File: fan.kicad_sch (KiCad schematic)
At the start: 18 parts, among them J5 Conn_01x04, J6 Conn_01x04, U16 TMP1075, U17 TMP1075, U18 EMC2302

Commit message: Resolved all unconnected pins, re-annotated, reviewed for layout
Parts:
- renumbered C62 to C31, C63 to C32, C64 to C33, C65 to C34, C66 to C35, C67 to C36, C68 to C37, R40 to R20, R41 to R21, TP9 to TP17, TP10 to TP18, TP11 to TP19, TP12 to TP20, U16 to U10, U17 to U11, U18 to U12

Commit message: Rough parts placement
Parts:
- TP17, TP18, TP19, TP20: footprint TestPoint:TestPoint_Pad_D1.5mm -> TestPoint:TestPoint_Pad_D1.0mm
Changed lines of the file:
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@@
       (effects (font (size 1.27 1.27)) (justify left) hide)
     )
-    (property "Footprint" "TestPoint:TestPoint_Pad_D1.5mm" (at 229.235 53.34 0)
+    (property "Footprint" "TestPoint:TestPoint_Pad_D1.0mm" (at 229.235 53.34 0)
       (effects (font (size 1.27 1.27)) hide)
     )
@@
       (effects (font (size 1.27 1.27)) (justify left) hide)
     )
-    (property "Footprint" "TestPoint:TestPoint_Pad_D1.5mm" (at 229.235 86.36 0)
+    (property "Footprint" "TestPoint:TestPoint_Pad_D1.0mm" (at 229.235 86.36 0)
       (effects (font (size 1.27 1.27)) hide)
     )
@@
       (effects (font (size 1.27 1.27)) (justify left) hide)
     )
-    (property "Footprint" "TestPoint:TestPoint_Pad_D1.5mm" (at 195.58 55.88 0)
+    (property "Footprint" "TestPoint:TestPoint_Pad_D1.0mm" (at 195.58 55.88 0)
       (effects (font (size 1.27 1.27)) hide)
     )
@@
       (effects (font (size 1.27 1.27)) (justify left) hide)
     )
-    (property "Footprint" "TestPoint:TestPoint_Pad_D1.5mm" (at 195.58 88.9 0)
-      (effects (font (size 1.27 1.27)) hide)
-    )
+    (property "Footprint" "TestPoint:TestPoint_Pad_D1.0mm" (at 195.58 88.9 0)
+      (effects (font (size 1.27 1.27)) hide)
+    )

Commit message: added some DK part numbers
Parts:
- U12: DK (none) -> EMC2302-2-AIZL-CT-ND; PARTNO (none) -> EMC2302-2-AIZL-TR
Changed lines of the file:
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@@
       (effects (font (size 1.27 1.27) italic) hide)
+    )
+    (property "DK" "EMC2302-2-AIZL-CT-ND" (at 89.535 52.07 0)
+      (effects (font (size 1.27 1.27)) hide)
+    )
+    (property "PARTNO" "EMC2302-2-AIZL-TR" (at 89.535 52.07 0)
+      (effects (font (size 1.27 1.27)) hide)
     )
     (pin "1")

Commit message: BOM mostly completed
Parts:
- R20, R21: DK (none) -> 13-RC0402FR-135K6LCT-ND; PARTNO (none) -> RC0402FR-135K6L
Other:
- title: bitaxeUltraHex -> bitaxeHex
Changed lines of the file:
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@@
   (paper "A")
   (title_block
-    (title "bitaxeUltraHex")
+    (title "bitaxeHex")
     (date "2023-06-11")
-    (rev "1")
+    (rev "300")
   )
   (junction (at 205.105 99.695) (diameter 0) (color 0 0 0 0)
@@
       (effects (font (size 1.27 1.27)) hide)
     )
-    (property "DK" "" (at 207.645 45.72 0)
-      (effects (font (size 1.27 1.27)) hide)
-    )
-    (property "PARTNO" "" (at 207.645 45.72 0)
+    (property "DK" "13-RC0402FR-135K6LCT-ND" (at 207.645 45.72 0)
+      (effects (font (size 1.27 1.27)) hide)
+    )
+    (property "PARTNO" "RC0402FR-135K6L" (at 207.645 45.72 0)
       (effects (font (size 1.27 1.27)) hide)
     )
@@
       (effects (font (size 1.27 1.27)) hide)
     )
-    (property "DK" "" (at 207.645 78.74 0)
-      (effects (font (size 1.27 1.27)) hide)
-    )
-    (property "PARTNO" "" (at 207.645 78.74 0)
-      (effects (font (size 1.27 1.27)) hide)
-    )
+    (property "DK" "13-RC0402FR-135K6LCT-ND" (at 207.645 78.74 0)
+      (effects (font (size 1.27 1.27)) hide)
+    )
+    (property "PARTNO" "RC0402FR-135K6L" (at 207.645 78.74 0)
+      (effects (font (size 1.27 1.27)) hide)
+    )

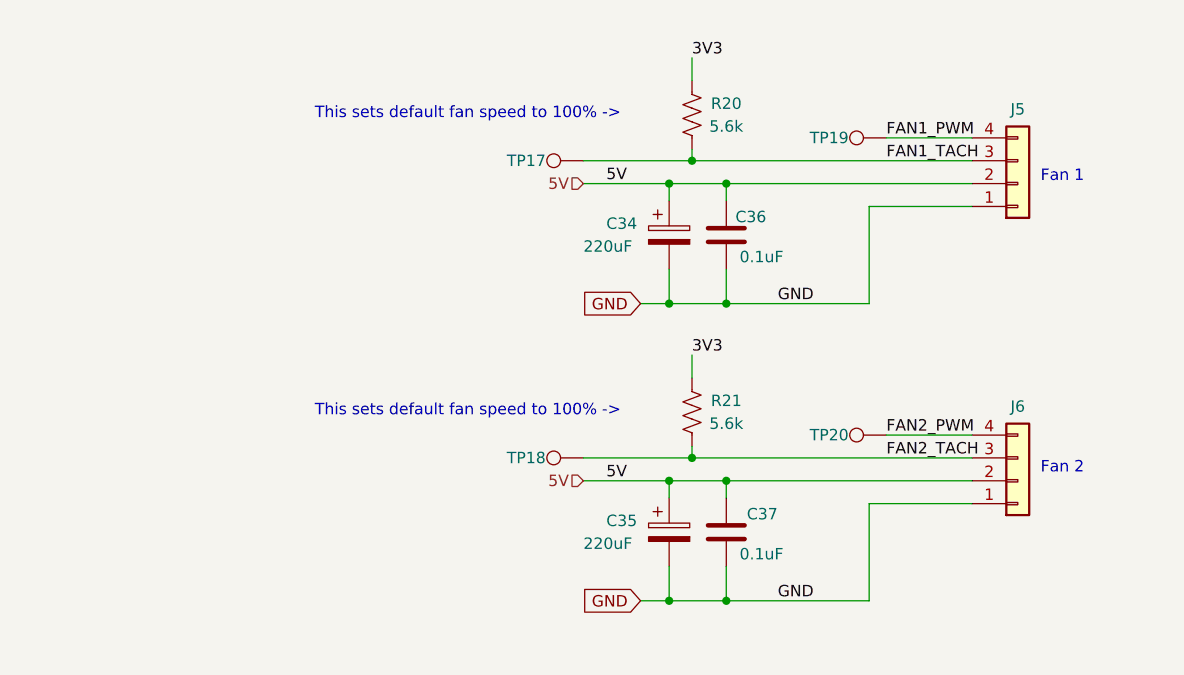
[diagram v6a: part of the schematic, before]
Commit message: remove old 5V power supply, prepare footprints for new 5V buck supply, switch fans to 12V
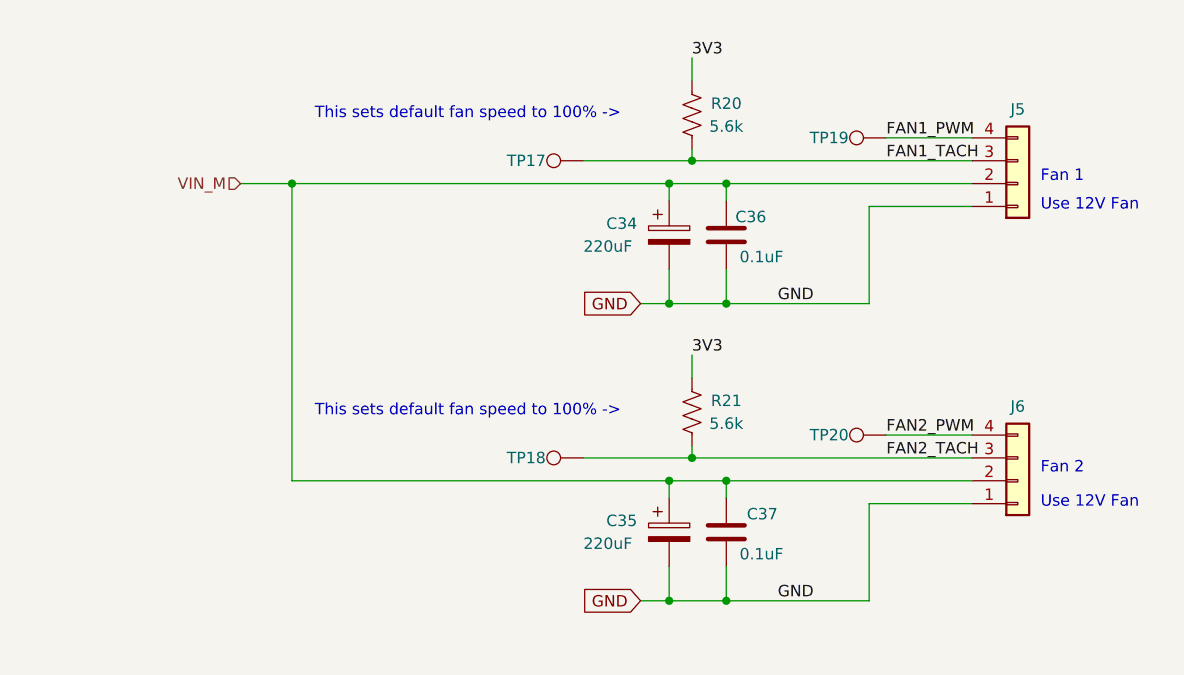
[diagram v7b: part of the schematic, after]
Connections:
- net 5V renamed VIN_M
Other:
- note added: "Use 12V Fan"
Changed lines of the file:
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@@
   (junction (at 105.41 120.65) (diameter 0) (color 0 0 0 0)
   )
+  (junction (at 163.195 53.34) (diameter 0) (color 0 0 0 0)
+  )
   (junction (at 105.41 137.795) (diameter 0) (color 0 0 0 0)
   )
@@
     (stroke (width 0) (type default))
   )
+  (wire (pts (xy 163.195 53.34) (xy 205.105 53.34))
+    (stroke (width 0) (type default))
+  )
   (wire (pts (xy 211.455 86.36) (xy 211.455 88.265))
     (stroke (width 0) (type default))
@@
     (stroke (width 0) (type default))
   )
+  (wire (pts (xy 163.195 86.36) (xy 163.195 53.34))
+    (stroke (width 0) (type default))
+  )
   (wire (pts (xy 211.455 99.695) (xy 227.33 99.695))
     (stroke (width 0) (type default))
@@
     (stroke (width 0) (type default))
   )
-  (wire (pts (xy 195.58 53.34) (xy 205.105 53.34))
+  (wire (pts (xy 157.48 53.34) (xy 163.195 53.34))
     (stroke (width 0) (type default))
   )
@@
     (stroke (width 0) (type default))
   )
-  (wire (pts (xy 195.58 86.36) (xy 205.105 86.36))
+  (wire (pts (xy 163.195 86.36) (xy 205.105 86.36))
     (stroke (width 0) (type default))
   )
@@
     (effects (font (size 1.27 1.27)) (justify left bottom))
   )
+  (text "Use 12V Fan" (at 246.38 56.515 0)
+    (effects (font (size 1.27 1.27)) (justify left bottom))
+  )
+  (text "Use 12V Fan" (at 246.38 89.535 0)
+    (effects (font (size 1.27 1.27)) (justify left bottom))
+  )
   (text "This sets default fan speed to 100% ->" (at 165.735 46.355 0)
     (effects (font (size 1.27 1.27)) (justify left bottom))
@@
     (effects (font (size 1.27 1.27)) (justify right bottom))
   )
-  (label "5V" (at 198.12 53.34 0) (fields_autoplaced)
-    (effects (font (size 1.27 1.27)) (justify left bottom))
-  )
   (label "3V3" (at 109.855 120.65 180) (fields_autoplaced)
     (effects (font (size 1.27 1.27)) (justify right bottom))
@@
   )
   (label "FAN2_PWM" (at 229.235 81.28 0) (fields_autoplaced)
-    (effects (font (size 1.27 1.27)) (justify left bottom))
-  )
-  (label "5V" (at 198.12 86.36 0) (fields_autoplaced)
     (effects (font (size 1.27 1.27)) (justify left bottom))
   )
@@
     )
   )
-  (hierarchical_label "5V" (shape input) (at 195.58 53.34 180) (fields_autoplaced)
+  (hierarchical_label "VIN_M" (shape input) (at 157.48 53.34 180) (fields_autoplaced)
     (effects (font (size 1.27 1.27)) (justify right))
   )
-  (hierarchical_label "5V" (shape input) (at 195.58 86.36 180) (fields_autoplaced)
-    (effects (font (size 1.27 1.27)) (justify right))
-  )

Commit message: BOM cleanup
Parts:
- C31, C32, C33, C36, C37: DK 1292-1639-1-ND -> 478-KGM05AR71C104KHCT-ND; PARTNO 0402X104K100CT -> KGM05AR71C104KH
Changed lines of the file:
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@@
       (effects (font (size 1.778 1.5113)) (justify left bottom) hide)
     )
-    (property "DK" "1292-1639-1-ND" (at 105.41 101.6 0)
-      (effects (font (size 1.27 1.27)) hide)
-    )
-    (property "PARTNO" "0402X104K100CT" (at 105.41 101.6 0)
+    (property "DK" "478-KGM05AR71C104KHCT-ND" (at 105.41 101.6 0)
+      (effects (font (size 1.27 1.27)) hide)
+    )
+    (property "PARTNO" "KGM05AR71C104KH" (at 105.41 101.6 0)
       (effects (font (size 1.27 1.27)) hide)
     )
@@
       (effects (font (size 1.778 1.5113)) (justify left bottom) hide)
     )
-    (property "DK" "1292-1639-1-ND" (at 57.785 52.07 0)
-      (effects (font (size 1.27 1.27)) hide)
-    )
-    (property "PARTNO" "0402X104K100CT" (at 57.785 52.07 0)
+    (property "DK" "478-KGM05AR71C104KHCT-ND" (at 57.785 52.07 0)
+      (effects (font (size 1.27 1.27)) hide)
+    )
+    (property "PARTNO" "KGM05AR71C104KH" (at 57.785 52.07 0)
       (effects (font (size 1.27 1.27)) hide)
     )
@@
       (effects (font (size 1.778 1.5113)) (justify left bottom) hide)
     )
-    (property "DK" "1292-1639-1-ND" (at 211.455 59.055 0)
-      (effects (font (size 1.27 1.27)) hide)
-    )
-    (property "PARTNO" "0402X104K100CT" (at 211.455 59.055 0)
+    (property "DK" "478-KGM05AR71C104KHCT-ND" (at 211.455 59.055 0)
+      (effects (font (size 1.27 1.27)) hide)
+    )
+    (property "PARTNO" "KGM05AR71C104KH" (at 211.455 59.055 0)
       (effects (font (size 1.27 1.27)) hide)
     )
@@
       (effects (font (size 1.778 1.5113)) (justify left bottom) hide)
     )
-    (property "DK" "1292-1639-1-ND" (at 211.455 92.075 0)
-      (effects (font (size 1.27 1.27)) hide)
-    )
-    (property "PARTNO" "0402X104K100CT" (at 211.455 92.075 0)
+    (property "DK" "478-KGM05AR71C104KHCT-ND" (at 211.455 92.075 0)
+      (effects (font (size 1.27 1.27)) hide)
+    )
+    (property "PARTNO" "KGM05AR71C104KH" (at 211.455 92.075 0)
       (effects (font (size 1.27 1.27)) hide)
     )
@@
       (effects (font (size 1.778 1.5113)) (justify left bottom) hide)
     )
-    (property "DK" "1292-1639-1-ND" (at 105.41 128.905 0)
-      (effects (font (size 1.27 1.27)) hide)
-    )
-    (property "PARTNO" "0402X104K100CT" (at 105.41 128.905 0)
-      (effects (font (size 1.27 1.27)) hide)
-    )
+    (property "DK" "478-KGM05AR71C104KHCT-ND" (at 105.41 128.905 0)
+      (effects (font (size 1.27 1.27)) hide)
+    )
+    (property "PARTNO" "KGM05AR71C104KH" (at 105.41 128.905 0)
+      (effects (font (size 1.27 1.27)) hide)
+    )
